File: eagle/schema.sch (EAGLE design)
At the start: 13 parts, among them IC1 LM1117T-3.3-V

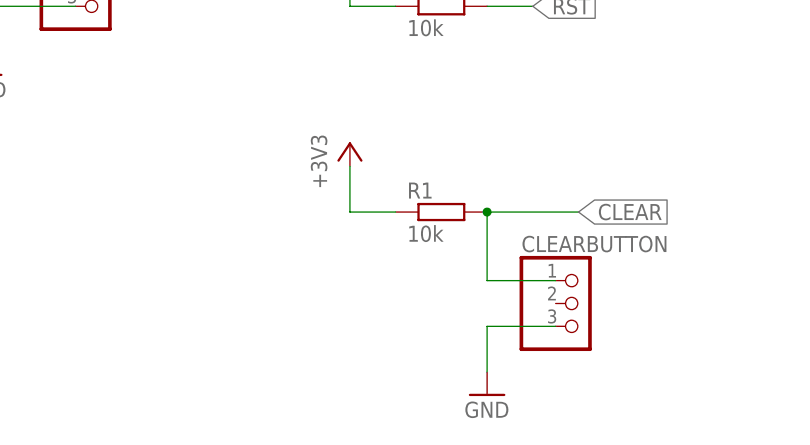
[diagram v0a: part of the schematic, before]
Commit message: added light sensor
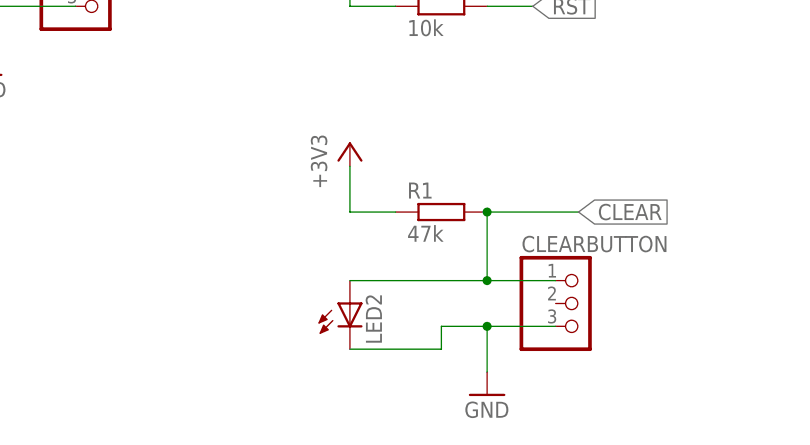
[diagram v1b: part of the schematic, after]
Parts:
- added LED2: (no value), led:LED3MM
- R1: value 10k -> 47k
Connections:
- net CLEAR: now also LED2.A
- net GND: now also LED2.C
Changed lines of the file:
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@@
 <part name="LED1" library="led" deviceset="LED" device="3MM"/>
 <part name="SENSORSOCKET" library="pinhead" deviceset="PINHD-1X3" device=""/>
-<part name="R1" library="rcl" deviceset="R-EU_" device="0204/5" value="10k"/>
+<part name="R1" library="rcl" deviceset="R-EU_" device="0204/5" value="47k"/>
 <part name="+3V4" library="supply1" deviceset="+3V3" device=""/>
 <part name="+3V5" library="supply1" deviceset="+3V3" device=""/>
@@
 <part name="CLEARBUTTON" library="pinhead" deviceset="PINHD-1X3" device=""/>
 <part name="P+3" library="supply1" deviceset="+5V" device=""/>
+<part name="LED2" library="led" deviceset="LED" device="3MM"/>
 </parts>
 <sheets>
@@
 <instance part="CLEARBUTTON" gate="A" x="111.76" y="2.54"/>
 <instance part="P+3" gate="1" x="45.72" y="50.8"/>
+<instance part="LED2" gate="G$1" x="86.36" y="2.54"/>
 </instances>
 <busses>
@@
 <pinref part="CLEARBUTTON" gate="A" pin="3"/>
 <wire x1="101.6" y1="0" x2="109.22" y2="0" width="0.1524" layer="91"/>
+<wire x1="101.6" y1="0" x2="96.52" y2="0" width="0.1524" layer="91"/>
+<wire x1="96.52" y1="0" x2="96.52" y2="-2.54" width="0.1524" layer="91"/>
+<pinref part="LED2" gate="G$1" pin="C"/>
+<wire x1="96.52" y1="-2.54" x2="86.36" y2="-2.54" width="0.1524" layer="91"/>
+<junction x="101.6" y="0"/>
 </segment>
 </net>
@@
 <wire x1="101.6" y1="5.08" x2="101.6" y2="12.7" width="0.1524" layer="91"/>
 <junction x="101.6" y="12.7"/>
-</segment>
-</net>
+<pinref part="LED2" gate="G$1" pin="A"/>
+<wire x1="86.36" y1="5.08" x2="101.6" y2="5.08" width="0.1524" layer="91"/>
+<junction x="101.6" y="5.08"/>
+</segment>
+</net>

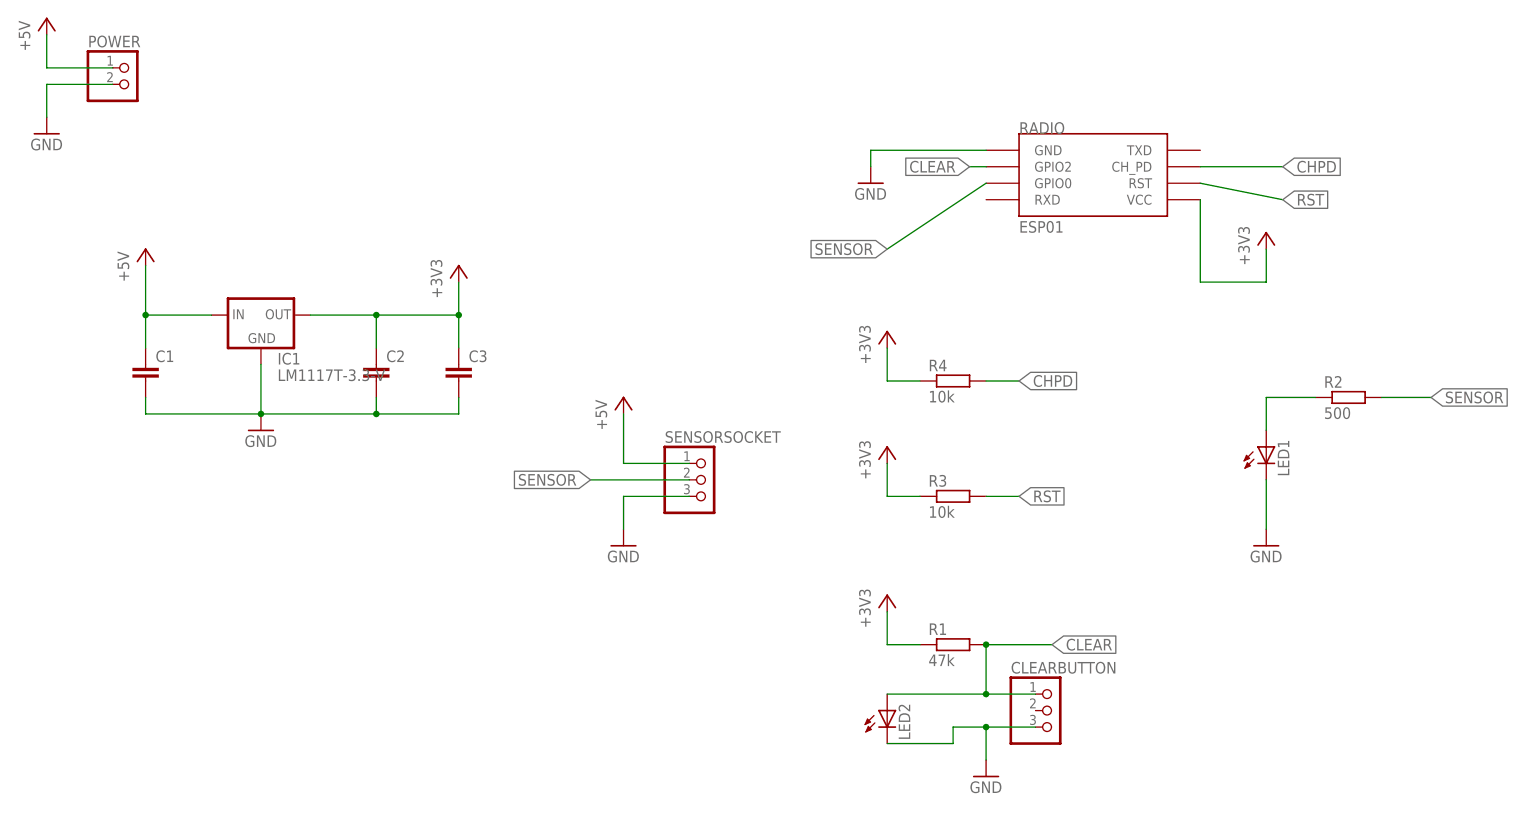
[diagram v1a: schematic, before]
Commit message: lights pin changed for well boot
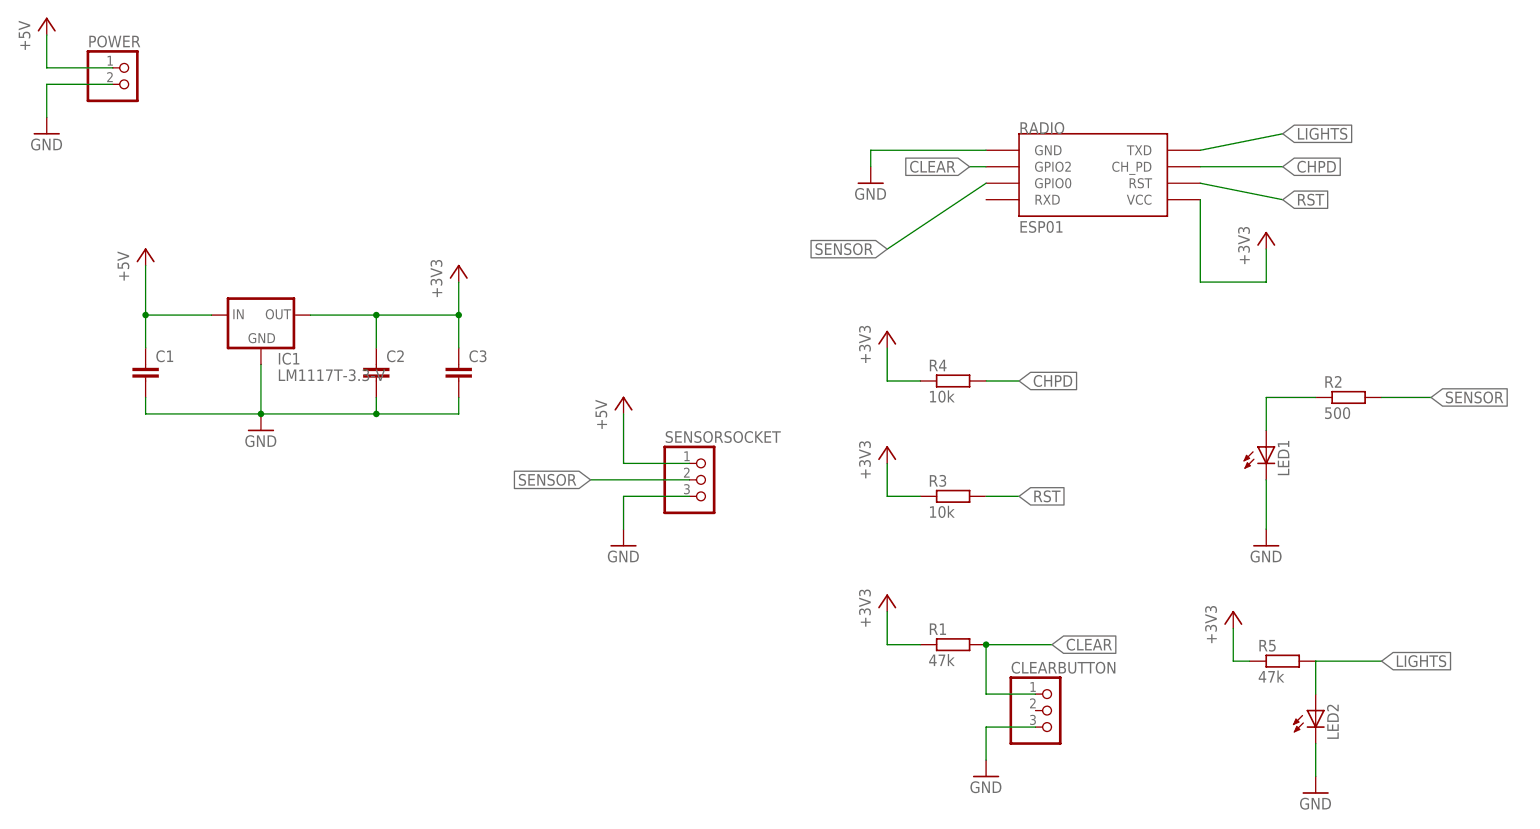
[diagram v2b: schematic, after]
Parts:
- added R5: 47k, rcl:R-EU_0204/5
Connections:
- new net LIGHTS: LED2.A, R5.2, RADIO.TXD
- net +3V3: now also R5.1
- net CLEAR: no longer LED2.A
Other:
- moved on the sheet: LED2
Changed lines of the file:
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@@
 <part name="P+3" library="supply1" deviceset="+5V" device=""/>
 <part name="LED2" library="led" deviceset="LED" device="3MM"/>
+<part name="+3V2" library="supply1" deviceset="+3V3" device=""/>
+<part name="GND5" library="supply1" deviceset="GND" device=""/>
+<part name="R5" library="rcl" deviceset="R-EU_" device="0204/5" value="47k"/>
 </parts>
 <sheets>
@@
 <instance part="CLEARBUTTON" gate="A" x="111.76" y="2.54"/>
 <instance part="P+3" gate="1" x="45.72" y="50.8"/>
-<instance part="LED2" gate="G$1" x="86.36" y="2.54"/>
+<instance part="LED2" gate="G$1" x="152.4" y="2.54"/>
+<instance part="+3V2" gate="G$1" x="139.7" y="17.78"/>
+<instance part="GND5" gate="1" x="152.4" y="-10.16"/>
+<instance part="R5" gate="G$1" x="147.32" y="10.16"/>
 </instances>
 <busses>
@@
 <pinref part="CLEARBUTTON" gate="A" pin="3"/>
 <wire x1="101.6" y1="0" x2="109.22" y2="0" width="0.1524" layer="91"/>
-<wire x1="101.6" y1="0" x2="96.52" y2="0" width="0.1524" layer="91"/>
-<wire x1="96.52" y1="0" x2="96.52" y2="-2.54" width="0.1524" layer="91"/>
+</segment>
+<segment>
 <pinref part="LED2" gate="G$1" pin="C"/>
-<wire x1="96.52" y1="-2.54" x2="86.36" y2="-2.54" width="0.1524" layer="91"/>
-<junction x="101.6" y="0"/>
+<pinref part="GND5" gate="1" pin="GND"/>
+<wire x1="152.4" y1="-2.54" x2="152.4" y2="-7.62" width="0.1524" layer="91"/>
 </segment>
 </net>
@@
 <wire x1="86.36" y1="12.7" x2="91.44" y2="12.7" width="0.1524" layer="91"/>
 </segment>
+<segment>
+<pinref part="+3V2" gate="G$1" pin="+3V3"/>
+<wire x1="139.7" y1="15.24" x2="139.7" y2="10.16" width="0.1524" layer="91"/>
+<pinref part="R5" gate="G$1" pin="1"/>
+<wire x1="139.7" y1="10.16" x2="142.24" y2="10.16" width="0.1524" layer="91"/>
+</segment>
 </net>
 <net name="CHPD" class="0">
@@
 <wire x1="101.6" y1="5.08" x2="101.6" y2="12.7" width="0.1524" layer="91"/>
 <junction x="101.6" y="12.7"/>
+</segment>
+</net>
+<net name="LIGHTS" class="0">
+<segment>
+<pinref part="RADIO" gate="G$1" pin="TXD"/>
+<wire x1="134.62" y1="88.9" x2="147.32" y2="91.44" width="0.1524" layer="91"/>
+<label x="147.32" y="91.44" size="1.778" layer="95" xref="yes"/>
+</segment>
+<segment>
+<pinref part="R5" gate="G$1" pin="2"/>
+<wire x1="152.4" y1="10.16" x2="152.4" y2="5.08" width="0.1524" layer="91"/>
 <pinref part="LED2" gate="G$1" pin="A"/>
-<wire x1="86.36" y1="5.08" x2="101.6" y2="5.08" width="0.1524" layer="91"/>
-<junction x="101.6" y="5.08"/>
-</segment>
-</net>
+<wire x1="152.4" y1="10.16" x2="162.56" y2="10.16" width="0.1524" layer="91"/>
+<label x="162.56" y="10.16" size="1.778" layer="95" xref="yes"/>
+</segment>
+</net>
